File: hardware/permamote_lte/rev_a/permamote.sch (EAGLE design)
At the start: 116 parts, among them IC1 NRF9160, J1 TC2030-JLINK-NL, J2 U.FL-R-SMT, J3 NANO_SIM, J4 U.FL-R-SMT, J5 DM3AT-SF-PEJM5, Q1 PMDXB950UPEL, Q10 PMDXB950UPEL, Q2 PMDXB950UPEL, Q3 PMDXB950UPEL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

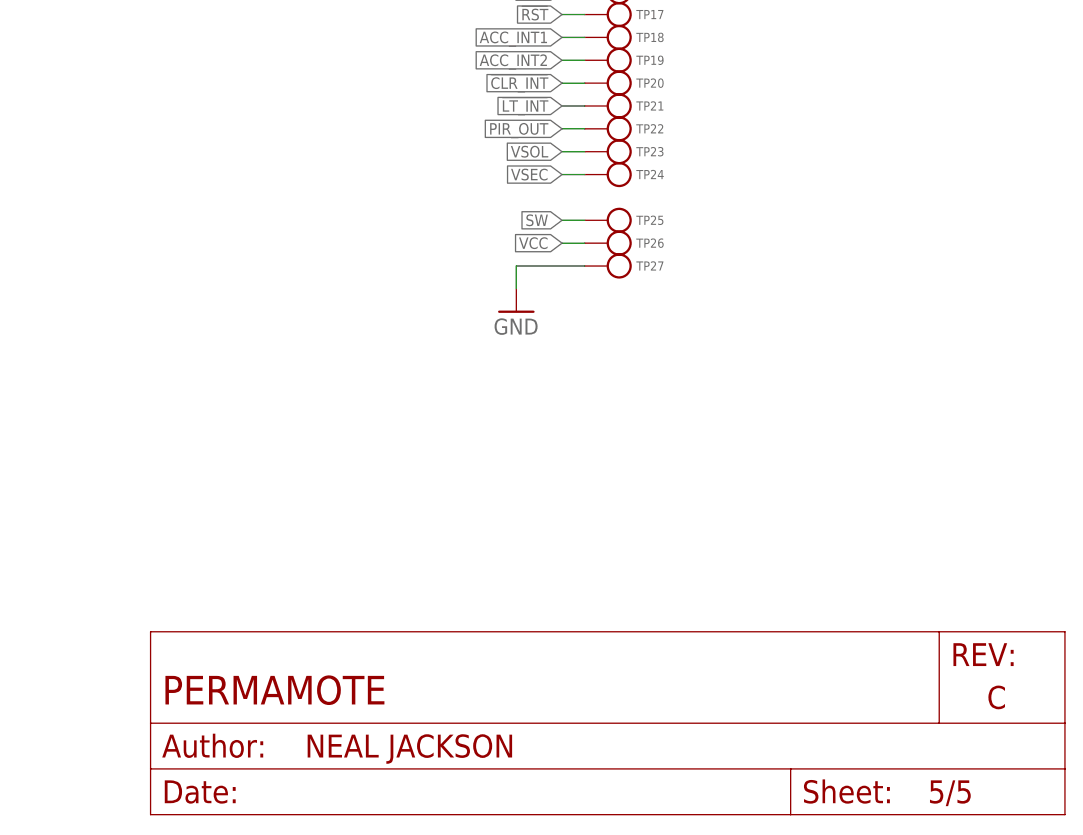
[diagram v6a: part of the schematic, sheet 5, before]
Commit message: made more changes but still having TPD3F303DPVR polygon issues
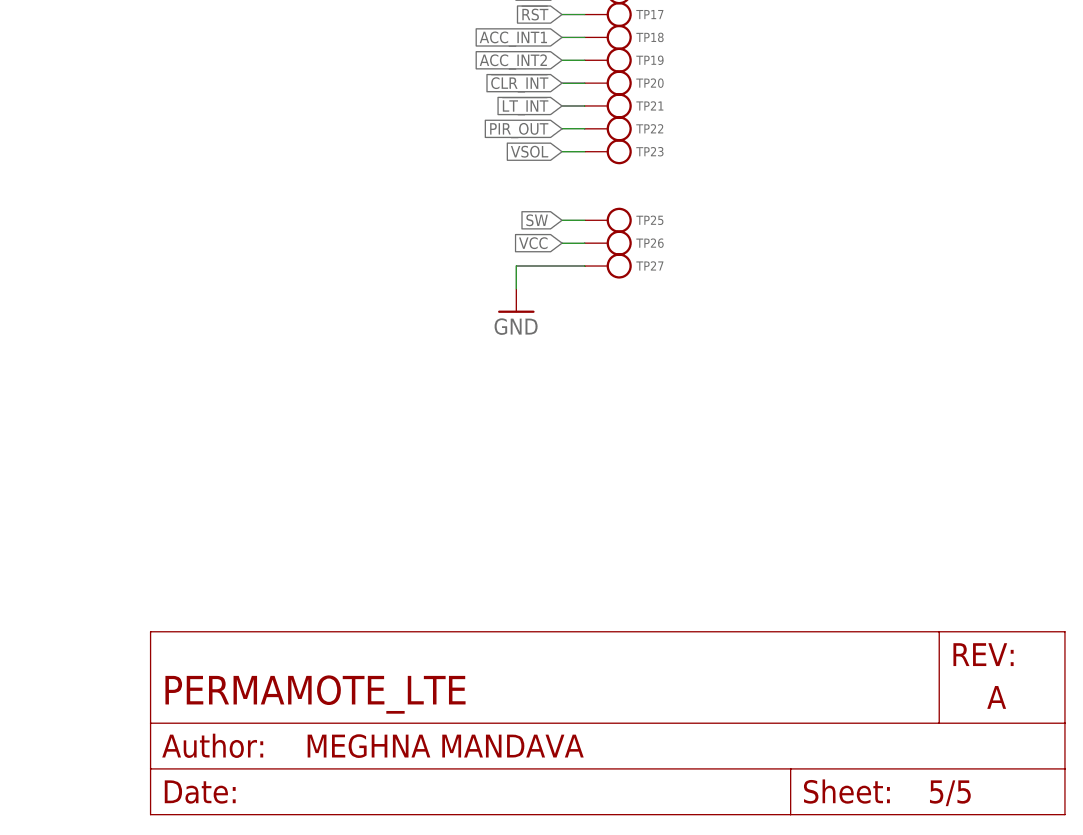
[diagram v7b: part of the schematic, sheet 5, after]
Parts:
- removed TP24: TEST-POINT, headers:TEST-POINT
- renumbered U5 to U13
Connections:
- removed net N$40: J3.C2(RST)
- net SIM_RST2: now also J3.C2(RST)
- net VSEC: no longer TP24.TESTPOINT
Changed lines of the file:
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@@
 <parts>
 <part name="FRAME1" library="lab11-frames" deviceset="LETTER_L_BLANK" device="">
+<attribute name="AUTHOR" value="MEGHNA MANDAVA"/>
 <attribute name="REV" value="A"/>
 <attribute name="TITLE" value="PERMAMOTE_LTE"/>
 </part>
 <part name="GND3" library="supply1" library_urn="urn:adsk.eagle:library:371" deviceset="GND" device=""/>
-<part name="FRAME2" library="lab11-frames" deviceset="LETTER_L_BLANK" device=""/>
+<part name="FRAME2" library="lab11-frames" deviceset="LETTER_L_BLANK" device="">
+<attribute name="AUTHOR" value="MEGHNA MANDAVA"/>
+<attribute name="REV" value="A"/>
+<attribute name="TITLE" value="PERMAMOTE_LTE"/>
+</part>
 <part name="U7" library="chips" deviceset="MAX17222" device=""/>
 <part name="C30" library="passives" deviceset="CAPACITOR" device="0603_CAP" value="10uF">
@@
 <part name="GND5" library="supply1" library_urn="urn:adsk.eagle:library:371" deviceset="GND" device=""/>
 <part name="P+4" library="mote" deviceset="VBAT" device=""/>
-<part name="FRAME3" library="lab11-frames" deviceset="LETTER_L_BLANK" device=""/>
+<part name="FRAME3" library="lab11-frames" deviceset="LETTER_L_BLANK" device="">
+<attribute name="AUTHOR" value="MEGHNA MANDAVA"/>
+<attribute name="REV" value="A"/>
+<attribute name="TITLE" value="PERMAMOTE_LTE"/>
+</part>
 <part name="U8" library="chips" deviceset="MAX44009" device=""/>
 <part name="C24" library="passives" deviceset="CAPACITOR" device="0402_CAP" value="1uF">
@@
 <part name="Q1" library="fets" deviceset="PMDXB950UPEL" device=""/>
 <part name="Q2" library="fets" deviceset="PMDXB950UPEL" device=""/>
-<part name="FRAME5" library="lab11-frames" deviceset="LETTER_L_BLANK" device=""/>
+<part name="FRAME5" library="lab11-frames" deviceset="LETTER_L_BLANK" device="">
+<attribute name="AUTHOR" value="MEGHNA MANDAVA"/>
+<attribute name="REV" value="A"/>
+<attribute name="TITLE" value="PERMAMOTE_LTE"/>
+</part>
 <part name="Q3" library="fets" deviceset="PMDXB950UPEL" device=""/>
 <part name="Q4" library="fets" deviceset="PMDXB950UPEL" device=""/>
@@
 <part name="TP22" library="headers" deviceset="TEST-POINT" device=""/>
 <part name="TP23" library="headers" deviceset="TEST-POINT" device=""/>
-<part name="TP24" library="headers" deviceset="TEST-POINT" device=""/>
 <part name="TP25" library="headers" deviceset="TEST-POINT" device=""/>
 <part name="TP26" library="headers" deviceset="TEST-POINT" device=""/>
@@
 <part name="L2" library="passives" deviceset="INDUCTOR" device="0402" value="5.1nH"/>
 <part name="L4" library="passives" deviceset="INDUCTOR" device="0402" value="1.8nH"/>
-<part name="U5" library="TPD3F303" deviceset="TPD3F303DPVR" device=""/>
 <part name="C1" library="passives" deviceset="CAPACITOR" device="0402_CAP" value="4.7uF">
 <attribute name="DESCRIPTION" value="CAP CER 4.7UF 10V X5R 0402"/>
@@
 <part name="+3V8" library="regulators" deviceset="+3V3" device=""/>
 <part name="FRAME4" library="lab11-frames" deviceset="LETTER_L_BLANK" device="">
+<attribute name="AUTHOR" value="MEGHNA MANDAVA"/>
 <attribute name="REV" value="A"/>
 <attribute name="TITLE" value="PERMAMOTE_LTE"/>
@@
 <part name="TP31" library="headers" deviceset="TEST-POINT" device=""/>
 <part name="TP32" library="headers" deviceset="TEST-POINT" device=""/>
+<part name="U13" library="TPD3F303" deviceset="TPD3F303DPVR" device=""/>
 </parts>
 <sheets>
@@
 </plain>
 <instances>
-<instance part="U5" gate="A" x="50.8" y="119.38" smashed="yes">
-<attribute name="NAME" x="58.7756" y="125.9586" size="2.0828" layer="95" ratio="6" rot="SR0"/>
-<attribute name="VALUE" x="58.1406" y="100.5586" size="2.0828" layer="96" ratio="6" rot="SR0"/>
-</instance>
 <instance part="J3" gate="G$1" x="187.96" y="111.76" smashed="yes">
 <attribute name="NAME" x="180.34" y="124.46" size="1.27" layer="95"/>
@@
 <attribute name="NAME" x="106.045" y="60.96" size="1.016" layer="95" ratio="12" align="center-right"/>
 </instance>
+<instance part="U13" gate="A" x="50.8" y="119.38" smashed="yes">
+<attribute name="NAME" x="58.7756" y="125.9586" size="2.0828" layer="95" ratio="6" rot="SR0"/>
+<attribute name="VALUE" x="58.1406" y="100.5586" size="2.0828" layer="96" ratio="6" rot="SR0"/>
+</instance>
 </instances>
 <busses>
@@
 <net name="SIM_1V8" class="0">
 <segment>
-<pinref part="U5" gate="A" pin="VCC"/>
 <wire x1="129.54" y1="109.22" x2="137.16" y2="109.22" width="0.1524" layer="91"/>
 <label x="137.16" y="109.22" size="1.27" layer="95" xref="yes"/>
+<pinref part="U13" gate="A" pin="VCC"/>
 </segment>
 <segment>
@@
 <net name="SIM_CLK" class="0">
 <segment>
-<pinref part="U5" gate="A" pin="CLK_IN"/>
 <wire x1="129.54" y1="114.3" x2="137.16" y2="114.3" width="0.1524" layer="91"/>
 <label x="137.16" y="114.3" size="1.27" layer="95" xref="yes"/>
+<pinref part="U13" gate="A" pin="CLK_IN"/>
 </segment>
 </net>
 <net name="SIM_IO" class="0">
 <segment>
-<pinref part="U5" gate="A" pin="DATA2_IN"/>
 <wire x1="129.54" y1="111.76" x2="137.16" y2="111.76" width="0.1524" layer="91"/>
 <label x="137.16" y="111.76" size="1.27" layer="95" xref="yes"/>
+<pinref part="U13" gate="A" pin="DATA2_IN"/>
 </segment>
 </net>
 <net name="SIM_RST2" class="0">
 <segment>
-<pinref part="U5" gate="A" pin="DATA1_OUT"/>
 <wire x1="53.34" y1="119.38" x2="50.8" y2="119.38" width="0.1524" layer="91"/>
 <label x="45.72" y="119.38" size="1.27" layer="95" rot="R180" xref="yes"/>
@@
 <junction x="50.8" y="119.38"/>
 <pinref part="TP30" gate="G$1" pin="TESTPOINT"/>
+<pinref part="U13" gate="A" pin="DATA1_OUT"/>
 </segment>
 <segment>
+<pinref part="J3" gate="G$1" pin="C2(RST)"/>
+<wire x1="175.26" y1="116.84" x2="172.72" y2="116.84" width="0.1524" layer="91"/>
 <label x="172.72" y="116.84" size="1.27" layer="95" rot="R180" xref="yes"/>
 </segment>
@@
 <net name="SIM_CLK2" class="0">
 <segment>
-<pinref part="U5" gate="A" pin="CLK_OUT"/>
 <wire x1="53.34" y1="116.84" x2="45.72" y2="116.84" width="0.1524" layer="91"/>
 <label x="45.72" y="116.84" size="1.27" layer="95" rot="R180" xref="yes"/>
+<pinref part="U13" gate="A" pin="CLK_OUT"/>
 </segment>
 <segment>
@@
 <net name="SIM_IO2" class="0">
 <segment>
-<pinref part="U5" gate="A" pin="DATA2_OUT"/>
 <wire x1="53.34" y1="114.3" x2="50.8" y2="114.3" width="0.1524" layer="91"/>
 <label x="45.72" y="114.3" size="1.27" layer="95" rot="R180" xref="yes"/>
@@
 <junction x="50.8" y="114.3"/>
 <pinref part="TP31" gate="G$1" pin="TESTPOINT"/>
+<pinref part="U13" gate="A" pin="DATA2_OUT"/>
 </segment>
 <segment>
@@
 <net name="SIM_RST" class="0">
 <segment>
-<pinref part="U5" gate="A" pin="DATA1_IN"/>
 <wire x1="129.54" y1="116.84" x2="137.16" y2="116.84" width="0.1524" layer="91"/>
 <label x="137.16" y="116.84" size="1.27" layer="95" xref="yes"/>
+<pinref part="U13" gate="A" pin="DATA1_IN"/>
 </segment>
 </net>
@@
 </segment>
 </net>
-<net name="N$40" class="0">
-<segment>
-<pinref part="J3" gate="G$1" pin="C2(RST)"/>
-<wire x1="175.26" y1="116.84" x2="172.72" y2="116.84" width="0.1524" layer="91"/>
-</segment>
-</net>
 <net name="MISO" class="0">
 <segment>
@@
 <attribute name="NAME" x="206.375" y="73.66" size="1.016" layer="95" ratio="12" rot="R180" align="center-right"/>
 </instance>
-<instance part="TP24" gate="G$1" x="203.2" y="71.12" smashed="yes" rot="R180">
-<attribute name="NAME" x="206.375" y="71.12" size="1.016" layer="95" ratio="12" rot="R180" align="center-right"/>
-</instance>
 <instance part="TP25" gate="G$1" x="203.2" y="66.04" smashed="yes" rot="R180">
 <attribute name="NAME" x="206.375" y="66.04" size="1.016" layer="95" ratio="12" rot="R180" align="center-right"/>
@@
 </segment>
 </net>
-<net name="VSEC" class="0">
-<segment>
-<wire x1="200.66" y1="71.12" x2="198.12" y2="71.12" width="0.1524" layer="91"/>
-<label x="198.12" y="71.12" size="1.27" layer="95" rot="R180" xref="yes"/>
-<pinref part="TP24" gate="G$1" pin="TESTPOINT"/>
-</segment>
-</net>

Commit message: before moving u10
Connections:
- removed net N$11: C4.2, J2.ANT
- removed net N$9: C3.1, IC1.ANT
- net GND: now also C3.1, C4.1, U1.VBAT
- net N$8: now also C4.2, IC1.ANT, J2.ANT; no longer C4.1
- net VBAT: no longer U1.VBAT
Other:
- moved on the sheet: C3, C4
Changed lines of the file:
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@@
 <part name="GND16" library="supply1" library_urn="urn:adsk.eagle:library:371" deviceset="GND" device=""/>
 <part name="P+12" library="mote" deviceset="VSW" device=""/>
-<part name="P+13" library="mote" deviceset="VBAT" device=""/>
 <part name="J1" library="connector" deviceset="TC2030-JLINK" device="-NL" value="TC2030-JLINK-NL"/>
 <part name="GND17" library="supply1" library_urn="urn:adsk.eagle:library:371" deviceset="GND" device=""/>
@@
 <part name="TP32" library="headers" deviceset="TEST-POINT" device=""/>
 <part name="U13" library="TPD3F303" deviceset="TPD3F303DPVR" device=""/>
+<part name="GND38" library="supply1" library_urn="urn:adsk.eagle:library:371" deviceset="GND" device=""/>
+<part name="GND39" library="supply1" library_urn="urn:adsk.eagle:library:371" deviceset="GND" device=""/>
+<part name="GND40" library="supply1" library_urn="urn:adsk.eagle:library:371" deviceset="GND" device=""/>
 </parts>
 <sheets>
@@
 <attribute name="VALUE" x="8.89" y="36.83" size="1.778" layer="96" ratio="12" rot="R270" align="bottom-center"/>
 </instance>
-<instance part="P+13" gate="VCC" x="48.26" y="48.26" smashed="yes">
-<attribute name="VALUE" x="45.72" y="45.72" size="1.778" layer="96" rot="R90"/>
-</instance>
 <instance part="J1" gate="G$1" x="177.8" y="83.82" smashed="yes">
 <attribute name="NAME" x="167.64" y="91.694" size="1.778" layer="95" ratio="12"/>
@@
 <attribute name="VALUE" x="58.42" y="88.9" size="1.778" layer="96"/>
 </instance>
-<instance part="C3" gate="G$1" x="154.94" y="129.54" smashed="yes" rot="R90">
-<attribute name="NAME" x="156.21" y="128.27" size="1.778" layer="95" ratio="12" rot="R180" align="bottom-center"/>
-<attribute name="VALUE" x="156.21" y="130.81" size="1.778" layer="96" ratio="12" align="bottom-center"/>
-</instance>
-<instance part="C4" gate="G$1" x="167.64" y="129.54" smashed="yes" rot="R90">
-<attribute name="NAME" x="168.91" y="128.27" size="1.778" layer="95" ratio="12" rot="R180" align="bottom-center"/>
-<attribute name="VALUE" x="168.91" y="130.81" size="1.778" layer="96" ratio="12" align="bottom-center"/>
+<instance part="C3" gate="G$1" x="154.94" y="124.46" smashed="yes" rot="R180">
+<attribute name="NAME" x="156.21" y="125.73" size="1.778" layer="95" ratio="12" rot="R270" align="bottom-center"/>
+<attribute name="VALUE" x="153.67" y="125.73" size="1.778" layer="96" ratio="12" rot="R90" align="bottom-center"/>
+</instance>
+<instance part="C4" gate="G$1" x="167.64" y="124.46" smashed="yes" rot="R180">
+<attribute name="NAME" x="168.91" y="125.73" size="1.778" layer="95" ratio="12" rot="R270" align="bottom-center"/>
+<attribute name="VALUE" x="166.37" y="125.73" size="1.778" layer="96" ratio="12" rot="R90" align="bottom-center"/>
 </instance>
 <instance part="GND33" gate="1" x="215.9" y="124.46" smashed="yes">
@@
 <attribute name="NAME" x="216.408" y="139.7" size="1.778" layer="95" ratio="12" rot="R270"/>
 <attribute name="VALUE" x="212.852" y="139.7" size="1.778" layer="96" ratio="12" rot="R270"/>
+</instance>
+<instance part="GND38" gate="1" x="48.26" y="38.1" smashed="yes">
+<attribute name="VALUE" x="45.72" y="35.56" size="1.778" layer="96"/>
+</instance>
+<instance part="GND39" gate="1" x="154.94" y="116.84" smashed="yes">
+<attribute name="VALUE" x="152.4" y="114.3" size="1.778" layer="96"/>
+</instance>
+<instance part="GND40" gate="1" x="167.64" y="116.84" smashed="yes">
+<attribute name="VALUE" x="165.1" y="114.3" size="1.778" layer="96"/>
 </instance>
 </instances>
@@
 <wire x1="185.42" y1="144.78" x2="185.42" y2="139.7" width="0.1524" layer="91"/>
 </segment>
+<segment>
+<pinref part="GND38" gate="1" pin="GND"/>
+<pinref part="U1" gate="G$1" pin="VBAT"/>
+<wire x1="48.26" y1="40.64" x2="50.8" y2="40.64" width="0.1524" layer="91"/>
+</segment>
+<segment>
+<pinref part="GND39" gate="1" pin="GND"/>
+<pinref part="C3" gate="G$1" pin="1"/>
+<wire x1="154.94" y1="119.38" x2="154.94" y2="121.92" width="0.1524" layer="91"/>
+</segment>
+<segment>
+<pinref part="GND40" gate="1" pin="GND"/>
+<pinref part="C4" gate="G$1" pin="1"/>
+<wire x1="167.64" y1="119.38" x2="167.64" y2="121.92" width="0.1524" layer="91"/>
+</segment>
 </net>
 <net name="VCC" class="0">
@@
 <pinref part="IC1" gate="G$1" pin="P0.15"/>
 </segment>
-<segment>
-<pinref part="U1" gate="G$1" pin="VBAT"/>
-<pinref part="P+13" gate="VCC" pin="VBAT"/>
-<wire x1="50.8" y1="40.64" x2="48.26" y2="40.64" width="0.1524" layer="91"/>
-<wire x1="48.26" y1="40.64" x2="48.26" y2="45.72" width="0.1524" layer="91"/>
-</segment>
 </net>
 <net name="SWDIO" class="0">
@@
 </segment>
 </net>
-<net name="N$8" class="0">
-<segment>
-<pinref part="C3" gate="G$1" pin="2"/>
-<pinref part="C4" gate="G$1" pin="1"/>
-<wire x1="160.02" y1="129.54" x2="165.1" y2="129.54" width="0.1524" layer="91"/>
-</segment>
-</net>
-<net name="N$9" class="0">
-<segment>
-<pinref part="C3" gate="G$1" pin="1"/>
-<pinref part="IC1" gate="G$1" pin="ANT"/>
-<wire x1="152.4" y1="129.54" x2="144.78" y2="129.54" width="0.1524" layer="91"/>
-</segment>
-</net>
-<net name="N$11" class="0">
-<segment>
-<pinref part="C4" gate="G$1" pin="2"/>
-<pinref part="J2" gate="G$1" pin="ANT"/>
-<wire x1="172.72" y1="129.54" x2="177.8" y2="129.54" width="0.1524" layer="91"/>
-</segment>
-</net>
 <net name="N$6" class="0">
 <segment>
@@
 <wire x1="144.78" y1="139.7" x2="144.78" y2="142.24" width="0.1524" layer="91"/>
 <wire x1="144.78" y1="139.7" x2="144.78" y2="144.78" width="0.1524" layer="91"/>
-<junction x="144.78" y="139.7"/>
 <wire x1="144.78" y1="144.78" x2="149.86" y2="144.78" width="0.1524" layer="91"/>
 </segment>
@@
 </segment>
 </net>
+<net name="N$8" class="0">
+<segment>
+<pinref part="IC1" gate="G$1" pin="ANT"/>
+<pinref part="C3" gate="G$1" pin="2"/>
+<wire x1="144.78" y1="129.54" x2="154.94" y2="129.54" width="0.1524" layer="91"/>
+<pinref part="C4" gate="G$1" pin="2"/>
+<wire x1="154.94" y1="129.54" x2="167.64" y2="129.54" width="0.1524" layer="91"/>
+<junction x="154.94" y="129.54"/>
+<pinref part="J2" gate="G$1" pin="ANT"/>
+<wire x1="167.64" y1="129.54" x2="177.8" y2="129.54" width="0.1524" layer="91"/>
+<junction x="167.64" y="129.54"/>
+</segment>
+</net>
